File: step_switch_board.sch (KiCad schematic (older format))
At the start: 75 parts

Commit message: adding switches and LEDs, SPI interface
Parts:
- removed C? (x2): 0.1µ, ~, symbol C_US
- removed D? (x16): LED, symbol LED
- removed R? (x2): 10K, ~, symbol R_US
- removed R? (x16): 470, ~, symbol R_US
- removed SW? (x8): TACT_SWITCH, symbol TACT_SWITCH
- removed U? (x2): 74AC595, symbol 74AC595
- added SW? (x8): TACT_SWITCH, symbol TACT_SWITCH
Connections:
- net labels added: SPI_SW_DATA
- net labels removed: +5V, LED_LATCH, SPI_MOSI, ~SPI_EN
- wire segments 245 -> 102
- no-connect marks 3 -> 2
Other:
- note removed: "SPI LED LATCH 1"
- note removed: "SPI LED LATCH 2"
- note removed: "SPI LED LATCH 3"
- note removed: "SPI_EN added to all 595s\nto keep LEDs off during\nMCU boot"

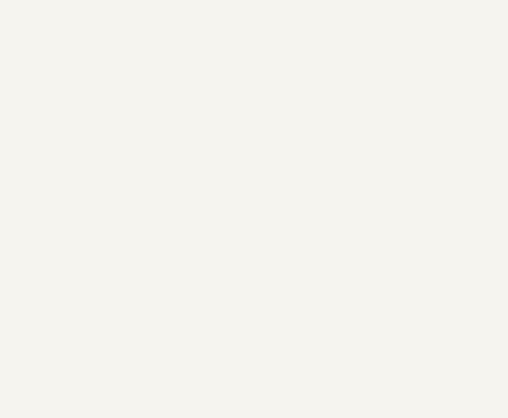
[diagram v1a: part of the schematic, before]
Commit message: updated ATMEGA328P to ATMEGA328PB. This is a newer MCU with slightly different pinout for VCC and GND. It's a little cheaper and has more timers
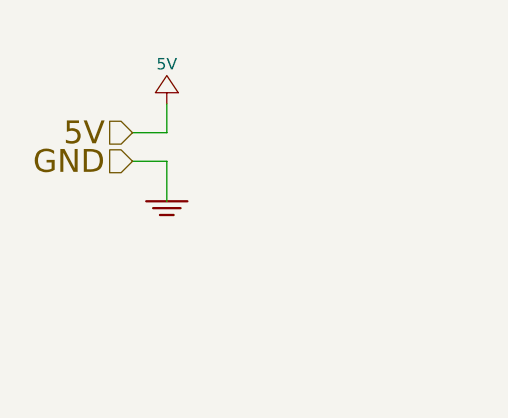
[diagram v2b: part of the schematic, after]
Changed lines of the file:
@@
 Text HLabel 10425 5275 0    60   Output ~ 0
 SPI_MISO
+Text HLabel 1400 1050 0    100  Input ~ 0
+5V
+Text HLabel 1400 1175 0    100  Input ~ 0
+GND
+$Comp
+L 5V #PWR?
+U 1 1 56B2ED48
+P 1550 925
+F 0 "#PWR?" H 1550 775 50  0001 C CNN
+F 1 "5V" H 1550 1100 50  0000 C CNN
+F 2 "" H 1550 925 60  0000 C CNN
+F 3 "" H 1550 925 60  0000 C CNN
+	1    1550 925
+	1    0    0    -1
+$EndComp
+Wire Wire Line
+	1400 1050 1550 1050
+Wire Wire Line
+	1550 1050 1550 925
+$Comp
+L GND_E #PWR?
+U 1 1 56B2F078
+P 1550 1350
+F 0 "#PWR?" V 1550 1350 30  0001 C CNN
+F 1 "GND_E" H 1550 1280 30  0001 C CNN
+F 2 "~" H 1550 1350 60  0000 C CNN
+F 3 "~" H 1550 1350 60  0000 C CNN
+	1    1550 1350
+	1    0    0    -1
+$EndComp
+Wire Wire Line
+	1400 1175 1550 1175
+Wire Wire Line
+	1550 1175 1550 1350
 $EndSCHEMATC

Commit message: more SPI work
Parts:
- added C? (x2): 0.1µ, ~, symbol C_US
- added D? (x16): LED, symbol LED
- added R?: 10K, ~, symbol R_US
- added R? (x16): 470, ~, symbol R_US
- added U? (x2): 74AC595, symbol 74AC595
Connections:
- net +5V: now also C?.1, C?.1, R?.1, U?.10 (~MR), U?.10 (~MR), U?.16 (VCC), U?.16 (VCC)
- net GND: now also C?.2, C?.2, D?.1 (K), D?.1 (K), D?.1 (K), D?.1 (K), D?.1 (K), D?.1 (K), D?.1 (K), D?.1 (K), D?.1 (K), D?.1 (K), D?.1 (K), D?.1 (K), D?.1 (K), D?.1 (K), D?.1 (K), D?.1 (K), U?.8 (GND), U?.8 (GND)
- net SPI_SCK: now also U?.11 (SCK), U?.11 (SCK)
- new net: D?.2 (A), R?.1 (x15)
- new net: R?.2, U?.2 (Q2) (x2)
- new net: R?.2, U?.1 (Q1) (x2)
- new net: R?.2, U?.5 (Q5) (x2)
- new net: R?.2, U?.4 (Q4) (x2)
- new net: R?.2, U?.3 (Q3) (x2)
- new net: R?.2, U?.15 (Q0) (x2)
- new net: R?.2, U?.6 (Q6) (x2)
- new net: R?.2, U?.7 (Q7) (x2)
- new net: U?.14 (SER), U?.9 (Q7S)
- new net LED_LATCH: U?.12 (RCK), U?.12 (RCK)
- new net SPI_MOSI: U?.14 (SER)
- new net ~SPI_EN: R?.2, U?.13 (~OE), U?.13 (~OE)
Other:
- note added: "SPI LED LATCH 1"
- note added: "SPI LED LATCH 2"
- note added: "SPI LED LATCH 3"
- note added: "SPI_EN added to all 595s\nto keep LEDs off during\nMCU boot"
- moved on the sheet: C?, R?, SW?, TP?, U?

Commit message: connecting up sequencer to step switch board, tidying up
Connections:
- net SPI_MISO is gone; now on net SPI_SW_DATA: TP?.1, U?.9 (Q7)
- net SPI_SW_DATA: no longer U?.10 (SER)
- net SPI_MOSI renamed SPI_LED_DATA
- no-connect marks 2 -> 4
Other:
- note removed: "SPI LED LATCH 3"
- note removed: "SPI_EN added to all 595s\nto keep LEDs off during\nMCU boot"
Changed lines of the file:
@@
 	7150 3675 7150 3775
 Wire Wire Line
-	6700 3200 6700 3275
-Wire Wire Line
-	6700 3275 6700 3775
+	6700 3200 6700 3775
 Wire Wire Line
 	7150 3275 6700 3275
 Wire Wire Line
-	6700 5675 6700 5700
-Wire Wire Line
-	6700 5700 6700 5775
+	6700 5675 6700 5775
 Wire Wire Line
 	7800 2575 7800 4275
@@
 	2625 3675 2625 3775
 Wire Wire Line
-	2175 3200 2175 3275
-Wire Wire Line
-	2175 3275 2175 3775
+	2175 3200 2175 3775
 Wire Wire Line
 	2625 3275 2175 3275
@@
 Connection ~ 7600 6025
 Wire Wire Line
-	3225 1775 3625 1775
-Wire Wire Line
-	3625 1775 4175 1775
-Wire Wire Line
-	3275 2575 3625 2575
-Wire Wire Line
-	3625 2575 4175 2575
-Wire Wire Line
-	3325 3375 3625 3375
-Wire Wire Line
-	3625 3375 4175 3375
-Wire Wire Line
-	3375 4175 3625 4175
-Wire Wire Line
-	3625 4175 4175 4175
-Wire Wire Line
-	3375 4975 3625 4975
-Wire Wire Line
-	3625 4975 4175 4975
-Wire Wire Line
-	3325 5775 3625 5775
-Wire Wire Line
-	3625 5775 4175 5775
-Wire Wire Line
-	3275 6575 3625 6575
-Wire Wire Line
-	3625 6575 4175 6575
-Wire Wire Line
-	3225 7375 3625 7375
-Wire Wire Line
-	3625 7375 4175 7375
-Wire Wire Line
-	7750 1775 8150 1775
-Wire Wire Line
-	8150 1775 8700 1775
-Wire Wire Line
-	7800 2575 8150 2575
-Wire Wire Line
-	8150 2575 8700 2575
-Wire Wire Line
-	7850 3375 8150 3375
-Wire Wire Line
-	8150 3375 8700 3375
-Wire Wire Line
-	7900 4175 8150 4175
-Wire Wire Line
-	8150 4175 8700 4175
-Wire Wire Line
-	7900 4975 8150 4975
-Wire Wire Line
-	8150 4975 8700 4975
-Wire Wire Line
-	7850 5775 8150 5775
-Wire Wire Line
-	8150 5775 8700 5775
-Wire Wire Line
-	7800 6575 8150 6575
-Wire Wire Line
-	8150 6575 8700 6575
-Wire Wire Line
-	7750 7375 8150 7375
-Wire Wire Line
-	8150 7375 8700 7375
+	3225 1775 4175 1775
+Wire Wire Line
+	3275 2575 4175 2575
+Wire Wire Line
+	3325 3375 4175 3375
+Wire Wire Line
+	3375 4175 4175 4175
+Wire Wire Line
+	3375 4975 4175 4975
+Wire Wire Line
+	3325 5775 4175 5775
+Wire Wire Line
+	3275 6575 4175 6575
+Wire Wire Line
+	3225 7375 4175 7375
+Wire Wire Line
+	7750 1775 8700 1775
+Wire Wire Line
+	7800 2575 8700 2575
+Wire Wire Line
+	7850 3375 8700 3375
+Wire Wire Line
+	7900 4175 8700 4175
+Wire Wire Line
+	7900 4975 8700 4975
+Wire Wire Line
+	7850 5775 8700 5775
+Wire Wire Line
+	7800 6575 8700 6575
+Wire Wire Line
+	7750 7375 8700 7375
 Wire Wire Line
 	5250 4175 5250 8500
@@
 P 4425 1775
 F 0 "SW?" V 4575 2000 50  0000 C CNN
-F 1 "TACT_SWITCH" V 4575 1325 50  0000 C CNN
+F 1 "TACT_SWITCH" V 4325 1775 50  0000 C CNN
 F 2 "" H 4425 1625 60  0000 C CNN
 F 3 "" H 4425 1625 60  0000 C CNN
@@
 P 4425 2575
 F 0 "SW?" V 4575 2800 50  0000 C CNN
-F 1 "TACT_SWITCH" V 4575 2125 50  0000 C CNN
+F 1 "TACT_SWITCH" V 4325 2575 50  0000 C CNN
 F 2 "" H 4425 2425 60  0000 C CNN
 F 3 "" H 4425 2425 60  0000 C CNN
@@
 P 4425 3375
 F 0 "SW?" V 4575 3600 50  0000 C CNN
-F 1 "TACT_SWITCH" V 4575 2925 50  0000 C CNN
+F 1 "TACT_SWITCH" V 4325 3375 50  0000 C CNN
 F 2 "" H 4425 3225 60  0000 C CNN
 F 3 "" H 4425 3225 60  0000 C CNN
@@
 P 4425 4175
 F 0 "SW?" V 4575 4400 50  0000 C CNN
-F 1 "TACT_SWITCH" V 4575 3725 50  0000 C CNN
+F 1 "TACT_SWITCH" V 4300 4175 50  0000 C CNN
 F 2 "" H 4425 4025 60  0000 C CNN
 F 3 "" H 4425 4025 60  0000 C CNN
@@
 P 4425 4975
 F 0 "SW?" V 4575 5200 50  0000 C CNN
-F 1 "TACT_SWITCH" V 4575 4525 50  0000 C CNN
+F 1 "TACT_SWITCH" V 4325 4975 50  0000 C CNN
 F 2 "" H 4425 4825 60  0000 C CNN
 F 3 "" H 4425 4825 60  0000 C CNN
@@
 P 4425 5775
 F 0 "SW?" V 4575 6000 50  0000 C CNN
-F 1 "TACT_SWITCH" V 4575 5325 50  0000 C CNN
+F 1 "TACT_SWITCH" V 4325 5775 50  0000 C CNN
 F 2 "" H 4425 5625 60  0000 C CNN
 F 3 "" H 4425 5625 60  0000 C CNN
@@
 P 4425 6575
 F 0 "SW?" V 4575 6800 50  0000 C CNN
-F 1 "TACT_SWITCH" V 4575 6125 50  0000 C CNN
+F 1 "TACT_SWITCH" V 4325 6575 50  0000 C CNN
 F 2 "" H 4425 6425 60  0000 C CNN
 F 3 "" H 4425 6425 60  0000 C CNN
@@
 P 4425 7375
 F 0 "SW?" V 4575 7600 50  0000 C CNN
-F 1 "TACT_SWITCH" V 4575 6925 50  0000 C CNN
+F 1 "TACT_SWITCH" V 4325 7375 50  0000 C CNN
 F 2 "" H 4425 7225 60  0000 C CNN
 F 3 "" H 4425 7225 60  0000 C CNN
@@
 $EndComp
 Wire Wire Line
-	4675 1525 4675 1775
-Wire Wire Line
-	4675 1775 4675 2575
-Wire Wire Line
-	4675 2575 4675 3375
-Wire Wire Line
-	4675 3375 4675 4175
-Wire Wire Line
-	4675 4175 4675 4975
-Wire Wire Line
-	4675 4975 4675 5775
-Wire Wire Line
-	4675 5775 4675 6575
-Wire Wire Line
-	4675 6575 4675 7375
+	4675 1525 4675 7375
 Connection ~ 4675 1775
 Connection ~ 4675 2575
@@
 P 8950 1775
 F 0 "SW?" V 9100 2000 50  0000 C CNN
-F 1 "TACT_SWITCH" V 9100 1325 50  0000 C CNN
+F 1 "TACT_SWITCH" V 8850 1775 50  0000 C CNN
 F 2 "" H 8950 1625 60  0000 C CNN
 F 3 "" H 8950 1625 60  0000 C CNN
@@
 P 8950 2575
 F 0 "SW?" V 9100 2800 50  0000 C CNN
-F 1 "TACT_SWITCH" V 9100 2125 50  0000 C CNN
+F 1 "TACT_SWITCH" V 8850 2575 50  0000 C CNN
 F 2 "" H 8950 2425 60  0000 C CNN
 F 3 "" H 8950 2425 60  0000 C CNN
@@
 P 8950 3375
 F 0 "SW?" V 9100 3600 50  0000 C CNN
-F 1 "TACT_SWITCH" V 9100 2925 50  0000 C CNN
+F 1 "TACT_SWITCH" V 8850 3375 50  0000 C CNN
 F 2 "" H 8950 3225 60  0000 C CNN
 F 3 "" H 8950 3225 60  0000 C CNN
@@
 P 8950 4175
 F 0 "SW?" V 9100 4400 50  0000 C CNN
-F 1 "TACT_SWITCH" V 9100 3725 50  0000 C CNN
+F 1 "TACT_SWITCH" V 8850 4175 50  0000 C CNN
 F 2 "" H 8950 4025 60  0000 C CNN
 F 3 "" H 8950 4025 60  0000 C CNN
@@
 P 8950 4975
 F 0 "SW?" V 9100 5200 50  0000 C CNN
-F 1 "TACT_SWITCH" V 9100 4525 50  0000 C CNN
+F 1 "TACT_SWITCH" V 8850 4975 50  0000 C CNN
 F 2 "" H 8950 4825 60  0000 C CNN
 F 3 "" H 8950 4825 60  0000 C CNN
@@
 P 8950 5775
 F 0 "SW?" V 9100 6000 50  0000 C CNN
-F 1 "TACT_SWITCH" V 9100 5325 50  0000 C CNN
+F 1 "TACT_SWITCH" V 8850 5775 50  0000 C CNN
 F 2 "" H 8950 5625 60  0000 C CNN
 F 3 "" H 8950 5625 60  0000 C CNN
@@
 P 8950 6575
 F 0 "SW?" V 9100 6800 50  0000 C CNN
-F 1 "TACT_SWITCH" V 9100 6125 50  0000 C CNN
+F 1 "TACT_SWITCH" V 8850 6575 50  0000 C CNN
 F 2 "" H 8950 6425 60  0000 C CNN
 F 3 "" H 8950 6425 60  0000 C CNN
@@
 P 8950 7375
 F 0 "SW?" V 9100 7600 50  0000 C CNN
-F 1 "TACT_SWITCH" V 9100 6925 50  0000 C CNN
+F 1 "TACT_SWITCH" V 8850 7375 50  0000 C CNN
 F 2 "" H 8950 7225 60  0000 C CNN
 F 3 "" H 8950 7225 60  0000 C CNN
@@
 $EndComp
 Wire Wire Line
-	9200 1525 9200 1775
-Wire Wire Line
-	9200 1775 9200 2575
-Wire Wire Line
-	9200 2575 9200 3375
-Wire Wire Line
-	9200 3375 9200 4175
-Wire Wire Line
-	9200 4175 9200 4975
-Wire Wire Line
-	9200 4975 9200 5775
-Wire Wire Line
-	9200 5775 9200 6575
-Wire Wire Line
-	9200 6575 9200 7375
+	9200 1525 9200 7375
 Connection ~ 9200 1775
 Connection ~ 9200 2575
@@
 Text HLabel 6000 4525 0    60   Input ~ 0
 SWITCH_LATCH
-Text HLabel 6000 4325 0    60   Input ~ 0
-SPI_SCK
 Text HLabel 1475 4525 0    60   Input ~ 0
 SWITCH_LATCH
-Text HLabel 1475 4325 0    60   Input ~ 0
+Text HLabel 1475 4325 0    60   BiDi ~ 0
 SPI_SCK
-Text HLabel 1475 4175 0    60   Input ~ 0
+Text HLabel 7450 6025 0    60   Output ~ 0
 SPI_SW_DATA
-Text HLabel 7450 6025 0    60   Output ~ 0
-SPI_MISO
 Text HLabel 1400 1050 0    100  Input ~ 0
 5V
@@
 Wire Wire Line
 	1550 1175 1550 1350
-Text GLabel 11650 2975 0    40   Input ~ 0
-SPI_MOSI
 $Comp
 L R_US R?
@@
 	1    0    0    -1
 $EndComp
-Text GLabel 11650 3425 0    40   Input ~ 0
-LED_LATCH
 $Comp
 L R_US R?
@@
 	1    0    0    -1
 $EndComp
-Text GLabel 11650 7075 0    40   Input ~ 0
-LED_LATCH
 $Comp
 L GND_E #PWR?
@@
 	1    0    0    -1
 $EndComp
-Text Notes 10600 2975 0    40   ~ 0
-SPI_EN added to all 595s\nto keep LEDs off during\nMCU boot
 Wire Wire Line
 	12800 2025 12800 2125
 Wire Wire Line
-	12350 1550 12350 1625
-Wire Wire Line
-	12350 1625 12350 1875
-Wire Wire Line
-	12350 1875 12350 2125
+	12350 1550 12350 2125
 Wire Wire Line
 	12800 1625 12350 1625
@@
 	13200 4525 13900 4525
 Wire Wire Line
-	11400 1875 11650 1875
-Wire Wire Line
-	11650 1875 12350 1875
+	11400 1875 12350 1875
 Wire Wire Line
 	11650 1875 11650 2525
@@
 	12800 5675 12800 5775
 Wire Wire Line
-	12350 5225 12350 5275
-Wire Wire Line
-	12350 5275 12350 5525
-Wire Wire Line
-	12350 5525 12350 5775
+	12350 5225 12350 5775
 Wire Wire Line
 	12800 5275 12350 5275
@@
 Connection ~ 12350 5525
 Wire Wire Line
-	15200 5025 15200 5475
-Wire Wire Line
-	15200 5475 15200 5925
-Wire Wire Line
-	15200 5925 15200 6375
-Wire Wire Line
-	15200 6375 15200 6825
-Wire Wire Line
-	15200 6825 15200 7275
-Wire Wire Line
-	15200 7275 15200 7725
-Wire Wire Line
-	15200 7725 15200 8175
-Wire Wire Line
-	15200 8175 15200 8425
+	15200 5025 15200 8425
 Wire Wire Line
 	14850 8175 15200 8175
@@
 	11150 4625 11150 6625
 Wire Wire Line
-	13050 7075 13050 8275
-Wire Wire Line
-	11250 2725 11400 2725
-Wire Wire Line
-	11400 2725 11650 2725
+	11250 2725 11650 2725
 Wire Wire Line
 	11400 2475 11400 2725
@@
 	11150 6625 11650 6625
 Wire Wire Line
-	13050 8275 11150 8275
-Wire Wire Line
-	11150 8275 11150 10325
-Wire Wire Line
 	14900 5025 15200 5025
 Wire Wire Line
 	11650 6375 11550 6375
-Text Notes 11200 8425 0    60   ~ 0
-SPI LED LATCH 3
 Text Notes 11200 4775 0    60   ~ 0
 SPI LED LATCH 2
@@
 $EndComp
 Wire Wire Line
-	15200 1375 15200 1825
-Wire Wire Line
-	15200 1825 15200 2275
-Wire Wire Line
-	15200 2275 15200 2725
-Wire Wire Line
-	15200 2725 15200 3175
-Wire Wire Line
-	15200 3175 15200 3625
-Wire Wire Line
-	15200 3625 15200 4075
-Wire Wire Line
-	15200 4075 15200 4525
-Wire Wire Line
-	15200 4525 15200 4775
+	15200 1375 15200 4775
 Wire Wire Line
 	14850 4525 15200 4525
@@
 Text HLabel 11550 6375 0    50   Input ~ 0
 ~SPI_EN
+NoConn ~ 13050 7075
+Text HLabel 11650 2975 0    50   Input ~ 0
+SPI_LED_DATA
+Text HLabel 6000 4325 0    60   BiDi ~ 0
+SPI_SCK
+Text HLabel 11650 3425 0    50   Input ~ 0
+LED_LATCH
+Text HLabel 11650 7075 0    50   Input ~ 0
+LED_LATCH
+NoConn ~ 1475 4175
 $EndSCHEMATC

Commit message: switch SPI set up, switches and LEDs given functional labels
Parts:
- D?: value LED -> STEP16
- D?: value LED -> STEP15
- D?: value LED -> STEP14
- D?: value LED -> STEP13
- D?: value LED -> STEP12
- D?: value LED -> STEP11
- D?: value LED -> STEP10
- D?: value LED -> STEP9
- D?: value LED -> STEP8
- D?: value LED -> STEP7
- D?: value LED -> STEP6
- D?: value LED -> STEP5
- D?: value LED -> STEP4
- D?: value LED -> STEP3
- D?: value LED -> STEP2
- D?: value LED -> STEP1
- SW?: value TACT_SWITCH -> STEP1
- SW?: value TACT_SWITCH -> STEP2
- SW?: value TACT_SWITCH -> STEP3
- SW?: value TACT_SWITCH -> STEP4
- SW?: value TACT_SWITCH -> STEP5
- SW?: value TACT_SWITCH -> STEP6
- SW?: value TACT_SWITCH -> STEP7
- SW?: value TACT_SWITCH -> STEP8
- SW?: value TACT_SWITCH -> STEP9
- SW?: value TACT_SWITCH -> STEP10
- SW?: value TACT_SWITCH -> STEP11
- SW?: value TACT_SWITCH -> STEP15
- SW?: value TACT_SWITCH -> STEP12
- SW?: value TACT_SWITCH -> STEP13
- SW?: value TACT_SWITCH -> STEP14
- SW?: value TACT_SWITCH -> STEP16
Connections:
- net at R?.2, U?.14 (D3): now also SW?.2; no longer SW?.2
- net at R?.2, U?.3 (D4): now also SW?.2; no longer SW?.2
- net at R?.2, U?.4 (D5): now also SW?.2; no longer SW?.2
- net at R?.2, U?.5 (D6): now also SW?.2; no longer SW?.2
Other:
- moved on the sheet: SW?
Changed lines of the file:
@@
 $Descr B 17000 11000
 encoding utf-8
-Sheet 3 4
+Sheet 4 4
 Title ""
 Date ""
@@
 P 4425 1775
 F 0 "SW?" V 4575 2000 50  0000 C CNN
-F 1 "TACT_SWITCH" V 4325 1775 50  0000 C CNN
+F 1 "STEP1" V 4325 1775 50  0000 C CNN
 F 2 "" H 4425 1625 60  0000 C CNN
 F 3 "" H 4425 1625 60  0000 C CNN
@@
 P 4425 2575
 F 0 "SW?" V 4575 2800 50  0000 C CNN
-F 1 "TACT_SWITCH" V 4325 2575 50  0000 C CNN
+F 1 "STEP2" V 4325 2575 50  0000 C CNN
 F 2 "" H 4425 2425 60  0000 C CNN
 F 3 "" H 4425 2425 60  0000 C CNN
@@
 P 4425 3375
 F 0 "SW?" V 4575 3600 50  0000 C CNN
-F 1 "TACT_SWITCH" V 4325 3375 50  0000 C CNN
+F 1 "STEP3" V 4325 3375 50  0000 C CNN
 F 2 "" H 4425 3225 60  0000 C CNN
 F 3 "" H 4425 3225 60  0000 C CNN
@@
 P 4425 4175
 F 0 "SW?" V 4575 4400 50  0000 C CNN
-F 1 "TACT_SWITCH" V 4300 4175 50  0000 C CNN
+F 1 "STEP4" V 4300 4175 50  0000 C CNN
 F 2 "" H 4425 4025 60  0000 C CNN
 F 3 "" H 4425 4025 60  0000 C CNN
@@
 P 4425 4975
 F 0 "SW?" V 4575 5200 50  0000 C CNN
-F 1 "TACT_SWITCH" V 4325 4975 50  0000 C CNN
+F 1 "STEP5" V 4325 4975 50  0000 C CNN
 F 2 "" H 4425 4825 60  0000 C CNN
 F 3 "" H 4425 4825 60  0000 C CNN
@@
 P 4425 5775
 F 0 "SW?" V 4575 6000 50  0000 C CNN
-F 1 "TACT_SWITCH" V 4325 5775 50  0000 C CNN
+F 1 "STEP6" V 4325 5775 50  0000 C CNN
 F 2 "" H 4425 5625 60  0000 C CNN
 F 3 "" H 4425 5625 60  0000 C CNN
@@
 P 4425 6575
 F 0 "SW?" V 4575 6800 50  0000 C CNN
-F 1 "TACT_SWITCH" V 4325 6575 50  0000 C CNN
+F 1 "STEP7" V 4325 6575 50  0000 C CNN
 F 2 "" H 4425 6425 60  0000 C CNN
 F 3 "" H 4425 6425 60  0000 C CNN
@@
 P 4425 7375
 F 0 "SW?" V 4575 7600 50  0000 C CNN
-F 1 "TACT_SWITCH" V 4325 7375 50  0000 C CNN
+F 1 "STEP8" V 4325 7375 50  0000 C CNN
 F 2 "" H 4425 7225 60  0000 C CNN
 F 3 "" H 4425 7225 60  0000 C CNN
@@
 P 8950 1775
 F 0 "SW?" V 9100 2000 50  0000 C CNN
-F 1 "TACT_SWITCH" V 8850 1775 50  0000 C CNN
+F 1 "STEP9" V 8850 1775 50  0000 C CNN
 F 2 "" H 8950 1625 60  0000 C CNN
 F 3 "" H 8950 1625 60  0000 C CNN
@@
 P 8950 2575
 F 0 "SW?" V 9100 2800 50  0000 C CNN
-F 1 "TACT_SWITCH" V 8850 2575 50  0000 C CNN
+F 1 "STEP10" V 8850 2575 50  0000 C CNN
 F 2 "" H 8950 2425 60  0000 C CNN
 F 3 "" H 8950 2425 60  0000 C CNN
@@
 P 8950 3375
 F 0 "SW?" V 9100 3600 50  0000 C CNN
-F 1 "TACT_SWITCH" V 8850 3375 50  0000 C CNN
+F 1 "STEP11" V 8850 3375 50  0000 C CNN
 F 2 "" H 8950 3225 60  0000 C CNN
 F 3 "" H 8950 3225 60  0000 C CNN
@@
 L TACT_SWITCH SW?
 U 1 1 56AA546E
+P 8950 6575
+F 0 "SW?" V 9100 6800 50  0000 C CNN
+F 1 "STEP15" V 8850 6575 50  0000 C CNN
+F 2 "" H 8950 6425 60  0000 C CNN
+F 3 "" H 8950 6425 60  0000 C CNN
+	1    8950 6575
+	0    -1   -1   0
+$EndComp
+$Comp
+L TACT_SWITCH SW?
+U 1 1 56AA5474
 P 8950 4175
 F 0 "SW?" V 9100 4400 50  0000 C CNN
-F 1 "TACT_SWITCH" V 8850 4175 50  0000 C CNN
+F 1 "STEP12" V 8850 4175 50  0000 C CNN
 F 2 "" H 8950 4025 60  0000 C CNN
 F 3 "" H 8950 4025 60  0000 C CNN
@@
 $Comp
 L TACT_SWITCH SW?
-U 1 1 56AA5474
+U 1 1 56AA547A
 P 8950 4975
 F 0 "SW?" V 9100 5200 50  0000 C CNN
-F 1 "TACT_SWITCH" V 8850 4975 50  0000 C CNN
+F 1 "STEP13" V 8850 4975 50  0000 C CNN
 F 2 "" H 8950 4825 60  0000 C CNN
 F 3 "" H 8950 4825 60  0000 C CNN
@@
 $Comp
 L TACT_SWITCH SW?
-U 1 1 56AA547A
+U 1 1 56AA5480
 P 8950 5775
 F 0 "SW?" V 9100 6000 50  0000 C CNN
-F 1 "TACT_SWITCH" V 8850 5775 50  0000 C CNN
+F 1 "STEP14" V 8850 5775 50  0000 C CNN
 F 2 "" H 8950 5625 60  0000 C CNN
 F 3 "" H 8950 5625 60  0000 C CNN
@@
 $Comp
 L TACT_SWITCH SW?
-U 1 1 56AA5480
-P 8950 6575
-F 0 "SW?" V 9100 6800 50  0000 C CNN
-F 1 "TACT_SWITCH" V 8850 6575 50  0000 C CNN
-F 2 "" H 8950 6425 60  0000 C CNN
-F 3 "" H 8950 6425 60  0000 C CNN
-	1    8950 6575
-	0    -1   -1   0
-$EndComp
-$Comp
-L TACT_SWITCH SW?
 U 1 1 56AA5486
 P 8950 7375
 F 0 "SW?" V 9100 7600 50  0000 C CNN
-F 1 "TACT_SWITCH" V 8850 7375 50  0000 C CNN
+F 1 "STEP16" V 8850 7375 50  0000 C CNN
 F 2 "" H 8950 7225 60  0000 C CNN
 F 3 "" H 8950 7225 60  0000 C CNN
@@
 P 14650 8175
 F 0 "D?" H 14650 8275 50  0000 C CNN
-F 1 "LED" H 14650 8075 50  0000 C CNN
+F 1 "STEP16" H 14650 8075 50  0000 C CNN
 F 2 "" H 14650 8175 60  0000 C CNN
 F 3 "" H 14650 8175 60  0000 C CNN
@@
 P 14650 7725
 F 0 "D?" H 14650 7825 50  0000 C CNN
-F 1 "LED" H 14650 7625 50  0000 C CNN
+F 1 "STEP15" H 14650 7625 50  0000 C CNN
 F 2 "" H 14650 7725 60  0000 C CNN
 F 3 "" H 14650 7725 60  0000 C CNN
@@
 P 14650 7275
 F 0 "D?" H 14650 7375 50  0000 C CNN
-F 1 "LED" H 14650 7175 50  0000 C CNN
+F 1 "STEP14" H 14650 7175 50  0000 C CNN
 F 2 "" H 14650 7275 60  0000 C CNN
 F 3 "" H 14650 7275 60  0000 C CNN
@@
 P 14650 6825
 F 0 "D?" H 14650 6925 50  0000 C CNN
-F 1 "LED" H 14650 6725 50  0000 C CNN
+F 1 "STEP13" H 14650 6725 50  0000 C CNN
 F 2 "" H 14650 6825 60  0000 C CNN
 F 3 "" H 14650 6825 60  0000 C CNN
@@
 P 14650 6375
 F 0 "D?" H 14650 6475 50  0000 C CNN
-F 1 "LED" H 14650 6275 50  0000 C CNN
+F 1 "STEP12" H 14650 6275 50  0000 C CNN
 F 2 "" H 14650 6375 60  0000 C CNN
 F 3 "" H 14650 6375 60  0000 C CNN
@@
 P 14650 5925
 F 0 "D?" H 14650 6025 50  0000 C CNN
-F 1 "LED" H 14650 5825 50  0000 C CNN
+F 1 "STEP11" H 14650 5825 50  0000 C CNN
 F 2 "" H 14650 5925 60  0000 C CNN
 F 3 "" H 14650 5925 60  0000 C CNN
@@
 P 14650 5475
 F 0 "D?" H 14650 5575 50  0000 C CNN
-F 1 "LED" H 14650 5375 50  0000 C CNN
+F 1 "STEP10" H 14650 5375 50  0000 C CNN
 F 2 "" H 14650 5475 60  0000 C CNN
 F 3 "" H 14650 5475 60  0000 C CNN
@@
 P 14700 5025
 F 0 "D?" H 14700 5125 50  0000 C CNN
-F 1 "LED" H 14700 4925 50  0000 C CNN
+F 1 "STEP9" H 14700 4925 50  0000 C CNN
 F 2 "" H 14700 5025 60  0000 C CNN
 F 3 "" H 14700 5025 60  0000 C CNN
@@
 P 14650 4525
 F 0 "D?" H 14650 4625 50  0000 C CNN
-F 1 "LED" H 14650 4425 50  0000 C CNN
+F 1 "STEP8" H 14650 4425 50  0000 C CNN
 F 2 "" H 14650 4525 60  0000 C CNN
 F 3 "" H 14650 4525 60  0000 C CNN
@@
 P 14650 4075
 F 0 "D?" H 14650 4175 50  0000 C CNN
-F 1 "LED" H 14650 3975 50  0000 C CNN
+F 1 "STEP7" H 14650 3975 50  0000 C CNN
 F 2 "" H 14650 4075 60  0000 C CNN
 F 3 "" H 14650 4075 60  0000 C CNN
@@
 P 14650 3625
 F 0 "D?" H 14650 3725 50  0000 C CNN
-F 1 "LED" H 14650 3525 50  0000 C CNN
+F 1 "STEP6" H 14650 3525 50  0000 C CNN
 F 2 "" H 14650 3625 60  0000 C CNN
 F 3 "" H 14650 3625 60  0000 C CNN
@@
 P 14650 3175
 F 0 "D?" H 14650 3275 50  0000 C CNN
-F 1 "LED" H 14650 3075 50  0000 C CNN
+F 1 "STEP5" H 14650 3075 50  0000 C CNN
 F 2 "" H 14650 3175 60  0000 C CNN
 F 3 "" H 14650 3175 60  0000 C CNN
@@
 P 14650 2725
 F 0 "D?" H 14650 2825 50  0000 C CNN
-F 1 "LED" H 14650 2625 50  0000 C CNN
+F 1 "STEP4" H 14650 2625 50  0000 C CNN
 F 2 "" H 14650 2725 60  0000 C CNN
 F 3 "" H 14650 2725 60  0000 C CNN
@@
 P 14650 2275
 F 0 "D?" H 14650 2375 50  0000 C CNN
-F 1 "LED" H 14650 2175 50  0000 C CNN
+F 1 "STEP3" H 14650 2175 50  0000 C CNN
 F 2 "" H 14650 2275 60  0000 C CNN
 F 3 "" H 14650 2275 60  0000 C CNN
@@
 P 14650 1825
 F 0 "D?" H 14650 1925 50  0000 C CNN
-F 1 "LED" H 14650 1725 50  0000 C CNN
+F 1 "STEP2" H 14650 1725 50  0000 C CNN
 F 2 "" H 14650 1825 60  0000 C CNN
 F 3 "" H 14650 1825 60  0000 C CNN
@@
 P 14700 1375
 F 0 "D?" H 14700 1475 50  0000 C CNN
-F 1 "LED" H 14700 1275 50  0000 C CNN
+F 1 "STEP1" H 14700 1275 50  0000 C CNN
 F 2 "" H 14700 1375 60  0000 C CNN
 F 3 "" H 14700 1375 60  0000 C CNN

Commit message: last commit before auto annotation
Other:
- note added: "SPI SWITCH LATCH 1"
- note added: "SPI SWITCH LATCH 2"
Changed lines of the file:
@@
 LED_LATCH
 NoConn ~ 1475 4175
+Text Notes 1025 3750 0    60   ~ 0
+SPI SWITCH LATCH 1
+Text Notes 5550 3725 0    60   ~ 0
+SPI SWITCH LATCH 2
 $EndSCHEMATC

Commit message: entire project annotaed, duplicate references fixed with '-1' suffix
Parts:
- gave numbers to parts that had none: 74
